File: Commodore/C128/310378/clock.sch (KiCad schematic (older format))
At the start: 14 parts, among them J1 C:PAL / O:NTSC, U16 74LS14, U28 8701, U29 7406, Y2 17.73447 MHz (PAL) / 14.31818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

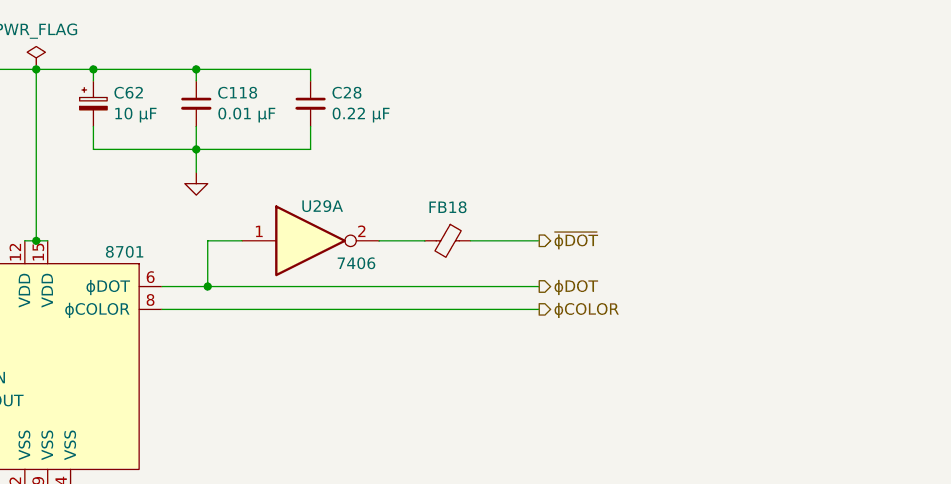
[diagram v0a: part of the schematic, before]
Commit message: Fix R47/R101 issue
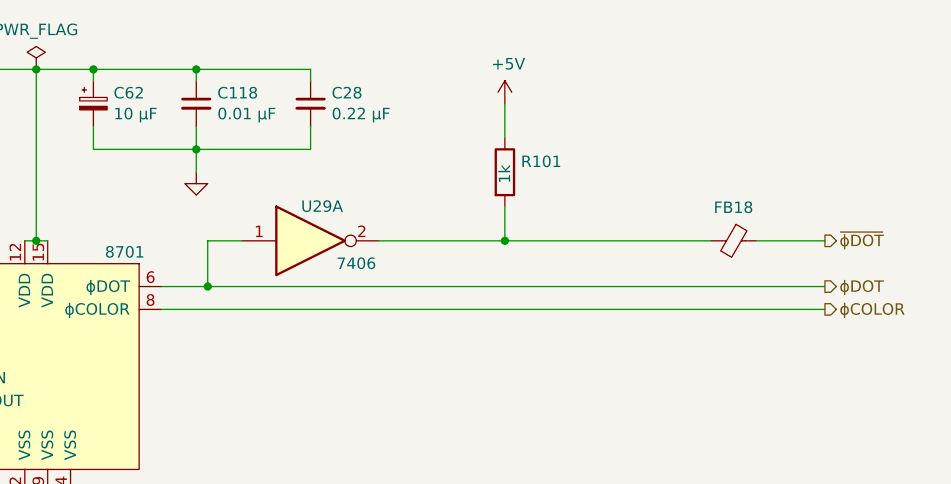
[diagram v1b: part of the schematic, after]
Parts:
- added R101: 1k, symbol Device:R
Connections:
- net +5V: now also R101.1
- net at FB18.2, U29.2: now also R101.2
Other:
- moved on the sheet: FB18
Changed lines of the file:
@@
 Wire Wire Line
 	2550 2950 2550 3000
-Text HLabel 5550 2050 2    50   Output ~ 0
+Text HLabel 6800 2050 2    50   Output ~ 0
 ϕCOLOR
 Wire Wire Line
-	3900 2050 5550 2050
-Text HLabel 5550 1950 2    50   Output ~ 0
+	3900 2050 6800 2050
+Text HLabel 6800 1950 2    50   Output ~ 0
 ϕDOT
 Wire Wire Line
@@
 	4100 1750 4250 1750
 Wire Wire Line
-	4100 1950 5550 1950
+	4100 1950 6800 1950
 $Comp
 L 74xx:74LS06 U29
@@
 	1    0    0    -1
 $EndComp
-Text HLabel 5550 1750 2    50   Output ~ 0
+Text HLabel 6800 1750 2    50   Output ~ 0
 ~ϕDOT
 Wire Wire Line
-	5550 1750 5250 1750
+	6800 1750 6500 1750
 Connection ~ 4100 1950
 $Comp
 L Device:Ferrite_Bead_Small FB18
 U 1 1 5DC5C94F
-P 5150 1750
-F 0 "FB18" V 5005 1750 50  0000 C CNN
-F 1 "Ferrite_Bead_Small" V 5004 1750 50  0001 C CNN
-F 2 "" V 5080 1750 50  0001 C CNN
-F 3 "~" H 5150 1750 50  0001 C CNN
-F 4 "81-BL02RN2R1M2B" H 5150 1750 50  0001 C CNN "Mouser Part"
-	1    5150 1750
+P 6400 1750
+F 0 "FB18" V 6255 1750 50  0000 C CNN
+F 1 "Ferrite_Bead_Small" V 6254 1750 50  0001 C CNN
+F 2 "" V 6330 1750 50  0001 C CNN
+F 3 "~" H 6400 1750 50  0001 C CNN
+F 4 "81-BL02RN2R1M2B" H 6400 1750 50  0001 C CNN "Mouser Part"
+	1    6400 1750
 	0    1    1    0
 $EndComp
 Wire Wire Line
-	5050 1750 4850 1750
+	6300 1750 5400 1750
 $Comp
 L power:PWR_FLAG #FLG0101
@@
 	3400 2850 3500 2850
 Connection ~ 3400 2850
+$Comp
+L Device:R R101
+U 1 1 60D93F87
+P 5400 1450
+F 0 "R101" H 5470 1496 50  0000 L CNN
+F 1 "1k" V 5400 1400 50  0000 L CNN
+F 2 "" V 5330 1450 50  0001 C CNN
+F 3 "~" H 5400 1450 50  0001 C CNN
+F 4 "660-MF1/4DCT52R5600F" H 5400 1450 50  0001 C CNN "Mouser Part"
+	1    5400 1450
+	1    0    0    -1
+$EndComp
+$Comp
+L power:+5V #PWR?
+U 1 1 60D94915
+P 5400 1150
+F 0 "#PWR?" H 5400 1000 50  0001 C CNN
+F 1 "+5V" H 5415 1323 50  0000 C CNN
+F 2 "" H 5400 1150 50  0001 C CNN
+F 3 "" H 5400 1150 50  0001 C CNN
+	1    5400 1150
+	1    0    0    -1
+$EndComp
+Wire Wire Line
+	5400 1150 5400 1300
+Wire Wire Line
+	5400 1600 5400 1750
+Connection ~ 5400 1750
+Wire Wire Line
+	5400 1750 4850 1750
 $EndSCHEMATC
